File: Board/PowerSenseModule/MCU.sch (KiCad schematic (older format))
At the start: 14 parts

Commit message: Using project library
Changed library ref to project not global
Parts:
- U?: symbol MCU_Microchip_CUSTOM:dsPIC33EP32GP502_QFN -> F1_Microchip_MCUs:dsPIC33EP32GP502_QFN
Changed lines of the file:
@@
 EESchema Schematic File Version 4
+LIBS:PowerSenseModule-cache
 EELAYER 29 0
 EELAYER END
@@
 	3650 1100 3600 1100
 $Comp
-L power:GND #PWR?
+L power:GND #PWR0101
 U 1 1 5D1B4504
 P 3800 1300
-F 0 "#PWR?" H 3800 1050 50  0001 C CNN
+F 0 "#PWR0101" H 3800 1050 50  0001 C CNN
 F 1 "GND" H 3805 1127 50  0000 C CNN
 F 2 "" H 3800 1300 50  0001 C CNN
@@
 $EndComp
 $Comp
-L power:GND #PWR?
+L power:GND #PWR0102
 U 1 1 5D1BA5A8
 P 1850 2400
-F 0 "#PWR?" H 1850 2150 50  0001 C CNN
+F 0 "#PWR0102" H 1850 2150 50  0001 C CNN
 F 1 "GND" H 1855 2227 50  0000 C CNN
 F 2 "" H 1850 2400 50  0001 C CNN
@@
 Connection ~ 3600 4200
 $Comp
-L power:GND #PWR?
+L power:GND #PWR0103
 U 1 1 5D1C8BCB
 P 3600 4200
-F 0 "#PWR?" H 3600 3950 50  0001 C CNN
+F 0 "#PWR0103" H 3600 3950 50  0001 C CNN
 F 1 "GND" H 3605 4027 50  0000 C CNN
 F 2 "" H 3600 4200 50  0001 C CNN
@@
 $EndComp
 $Comp
-L power:+5V #PWR?
+L power:+5V #PWR0104
 U 1 1 5D1D3CD9
 P 7000 1000
-F 0 "#PWR?" H 7000 850 50  0001 C CNN
+F 0 "#PWR0104" H 7000 850 50  0001 C CNN
 F 1 "+5V" H 7050 1150 50  0000 C CNN
 F 2 "" H 7000 1000 50  0001 C CNN
@@
 $EndComp
 $Comp
-L power:+3.3V #PWR?
+L power:+3.3V #PWR0105
 U 1 1 5D1D4392
 P 6900 1000
-F 0 "#PWR?" H 6900 850 50  0001 C CNN
+F 0 "#PWR0105" H 6900 850 50  0001 C CNN
 F 1 "+3.3V" H 6850 1150 50  0000 C CNN
 F 2 "" H 6900 1000 50  0001 C CNN
@@
 CANL
 $Comp
-L power:GND #PWR?
+L power:GND #PWR0106
 U 1 1 5D1D8E02
 P 7000 1800
-F 0 "#PWR?" H 7000 1550 50  0001 C CNN
+F 0 "#PWR0106" H 7000 1550 50  0001 C CNN
 F 1 "GND" H 7005 1627 50  0000 C CNN
 F 2 "" H 7000 1800 50  0001 C CNN
@@
 $EndComp
 $Comp
-L power:+3.3V #PWR?
+L power:+3.3V #PWR0107
 U 1 1 5D1E7B70
 P 1850 1400
-F 0 "#PWR?" H 1850 1250 50  0001 C CNN
+F 0 "#PWR0107" H 1850 1250 50  0001 C CNN
 F 1 "+3.3V" H 1865 1573 50  0000 C CNN
 F 2 "" H 1850 1400 50  0001 C CNN
@@
 $EndComp
 $Comp
-L power:+3.3V #PWR?
+L power:+3.3V #PWR0108
 U 1 1 5D1E7EFD
 P 3300 950
-F 0 "#PWR?" H 3300 800 50  0001 C CNN
+F 0 "#PWR0108" H 3300 800 50  0001 C CNN
 F 1 "+3.3V" H 3315 1123 50  0000 C CNN
 F 2 "" H 3300 950 50  0001 C CNN
@@
 $EndComp
 $Comp
-L power:+3.3V #PWR?
+L power:+3.3V #PWR0109
 U 1 1 5D1E73B5
 P 8050 2350
-F 0 "#PWR?" H 8050 2200 50  0001 C CNN
+F 0 "#PWR0109" H 8050 2200 50  0001 C CNN
 F 1 "+3.3V" H 8065 2523 50  0000 C CNN
 F 2 "" H 8050 2350 50  0001 C CNN
@@
 Close to VDD MCU pin\n
 $Comp
-L power:GND #PWR?
+L power:GND #PWR0110
 U 1 1 5D1BE44C
 P 8050 2650
-F 0 "#PWR?" H 8050 2400 50  0001 C CNN
+F 0 "#PWR0110" H 8050 2400 50  0001 C CNN
 F 1 "GND" H 8055 2477 50  0000 C CNN
 F 2 "" H 8050 2650 50  0001 C CNN
@@
 Close to CAN transceiver
 $Comp
-L power:GND #PWR?
+L power:GND #PWR0111
 U 1 1 5D1E97C4
 P 9500 2650
-F 0 "#PWR?" H 9500 2400 50  0001 C CNN
+F 0 "#PWR0111" H 9500 2400 50  0001 C CNN
 F 1 "GND" H 9505 2477 50  0000 C CNN
 F 2 "" H 9500 2650 50  0001 C CNN
@@
 $EndComp
 $Comp
-L power:+5V #PWR?
+L power:+5V #PWR0112
 U 1 1 5D1E9E31
 P 9500 2350
-F 0 "#PWR?" H 9500 2200 50  0001 C CNN
+F 0 "#PWR0112" H 9500 2200 50  0001 C CNN
 F 1 "+5V" H 9515 2523 50  0000 C CNN
 F 2 "" H 9500 2350 50  0001 C CNN
@@
 $EndComp
 $Comp
-L power:+3.3V #PWR?
+L power:+3.3V #PWR0113
 U 1 1 5D1EE46F
 P 9100 1200
-F 0 "#PWR?" H 9100 1050 50  0001 C CNN
+F 0 "#PWR0113" H 9100 1050 50  0001 C CNN
 F 1 "+3.3V" H 9115 1373 50  0000 C CNN
 F 2 "" H 9100 1200 50  0001 C CNN
@@
 $EndComp
 $Comp
-L power:GND #PWR?
+L power:GND #PWR0114
 U 1 1 5D1EF94D
 P 9100 1450
-F 0 "#PWR?" H 9100 1200 50  0001 C CNN
+F 0 "#PWR0114" H 9100 1200 50  0001 C CNN
 F 1 "GND" H 9105 1277 50  0000 C CNN
 F 2 "" H 9100 1450 50  0001 C CNN
@@
 	9100 1400 9100 1450
 $Comp
-L power:GND #PWR?
+L power:GND #PWR0115
 U 1 1 5D1F1BB9
 P 9550 1700
-F 0 "#PWR?" H 9550 1450 50  0001 C CNN
+F 0 "#PWR0115" H 9550 1450 50  0001 C CNN
 F 1 "GND" H 9555 1527 50  0000 C CNN
 F 2 "" H 9550 1700 50  0001 C CNN
@@
 	1700 1800 1850 1800
 $Comp
-L MCU_Microchip_CUSTOM:dsPIC33EP32GP502_QFN U?
+L F1_Microchip_MCUs:dsPIC33EP32GP502_QFN U?
 U 1 1 5D1D3BA4
 P 2450 3900

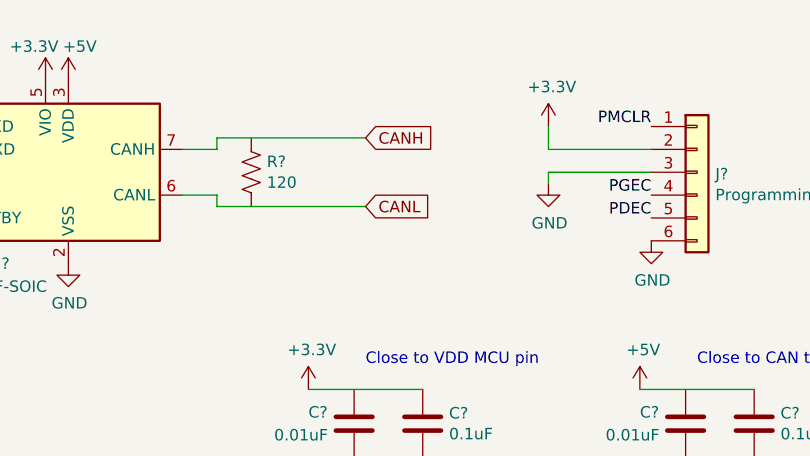
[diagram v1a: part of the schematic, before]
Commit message: Changed power connector and added CAN nets
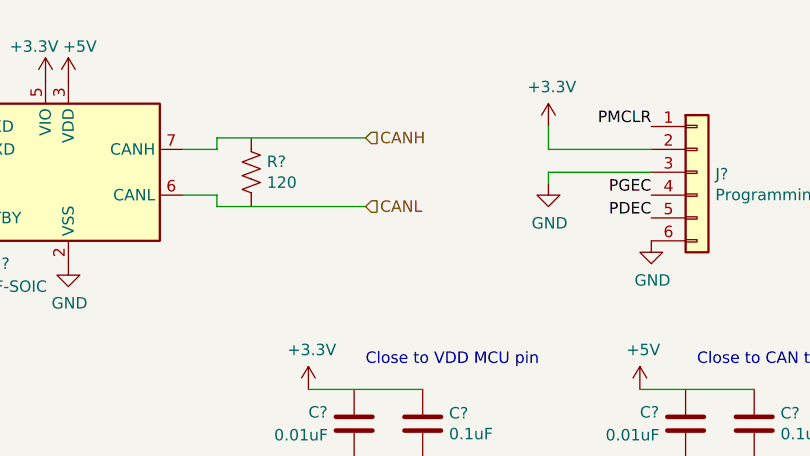
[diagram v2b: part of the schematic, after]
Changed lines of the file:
@@
 Wire Wire Line
 	7650 1500 7650 1550
-Text GLabel 8300 1250 2    50   Input ~ 0
-CANH
-Text GLabel 8300 1550 2    50   Input ~ 0
-CANL
 $Comp
 L power:GND #PWR0106
@@
 Text Label 9550 1200 2    50   ~ 0
 PMCLR
+Text HLabel 8300 1250 2    50   Input ~ 0
+CANH
+Text HLabel 8300 1550 2    50   Input ~ 0
+CANL
 $EndSCHEMATC

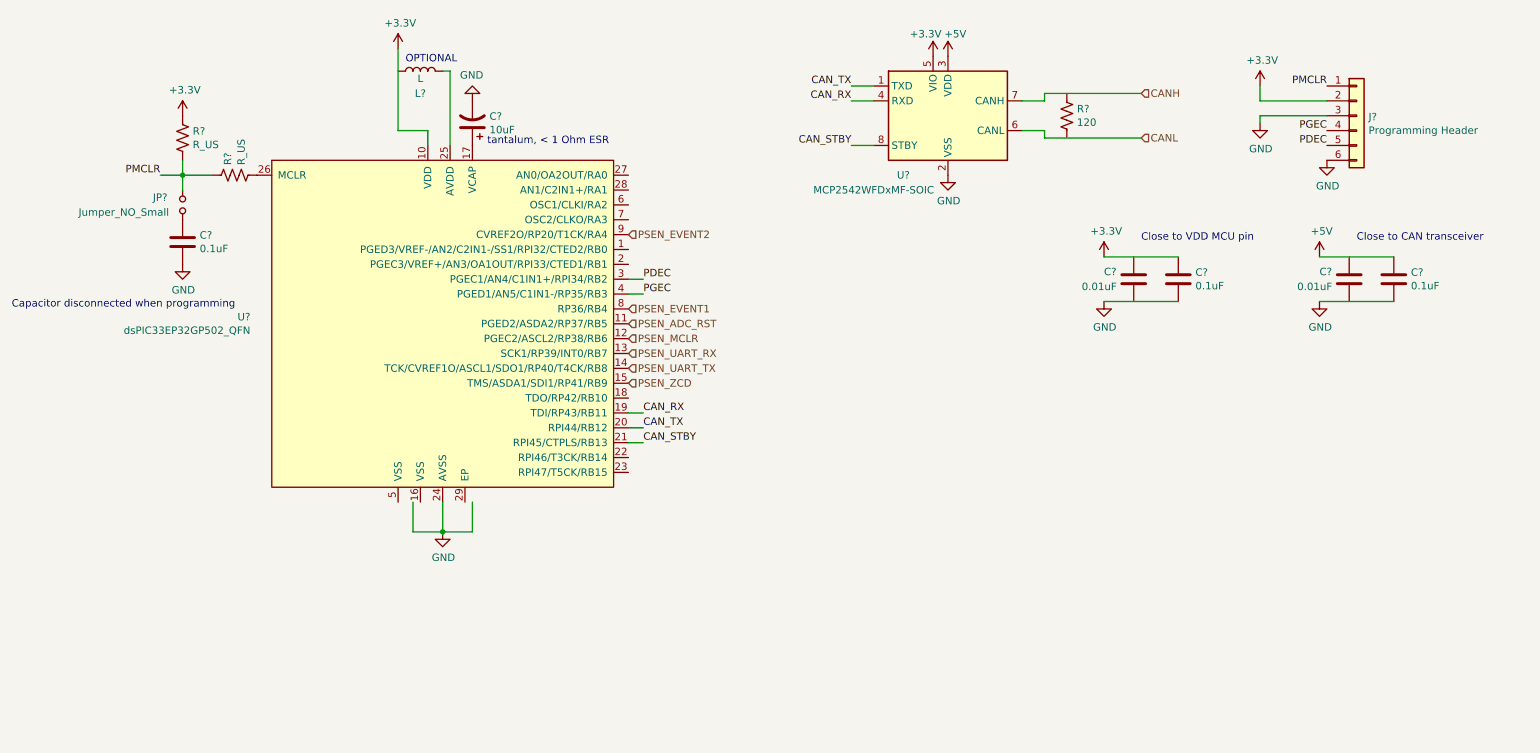
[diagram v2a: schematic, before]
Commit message: Added linear reg, cleaned up schematic
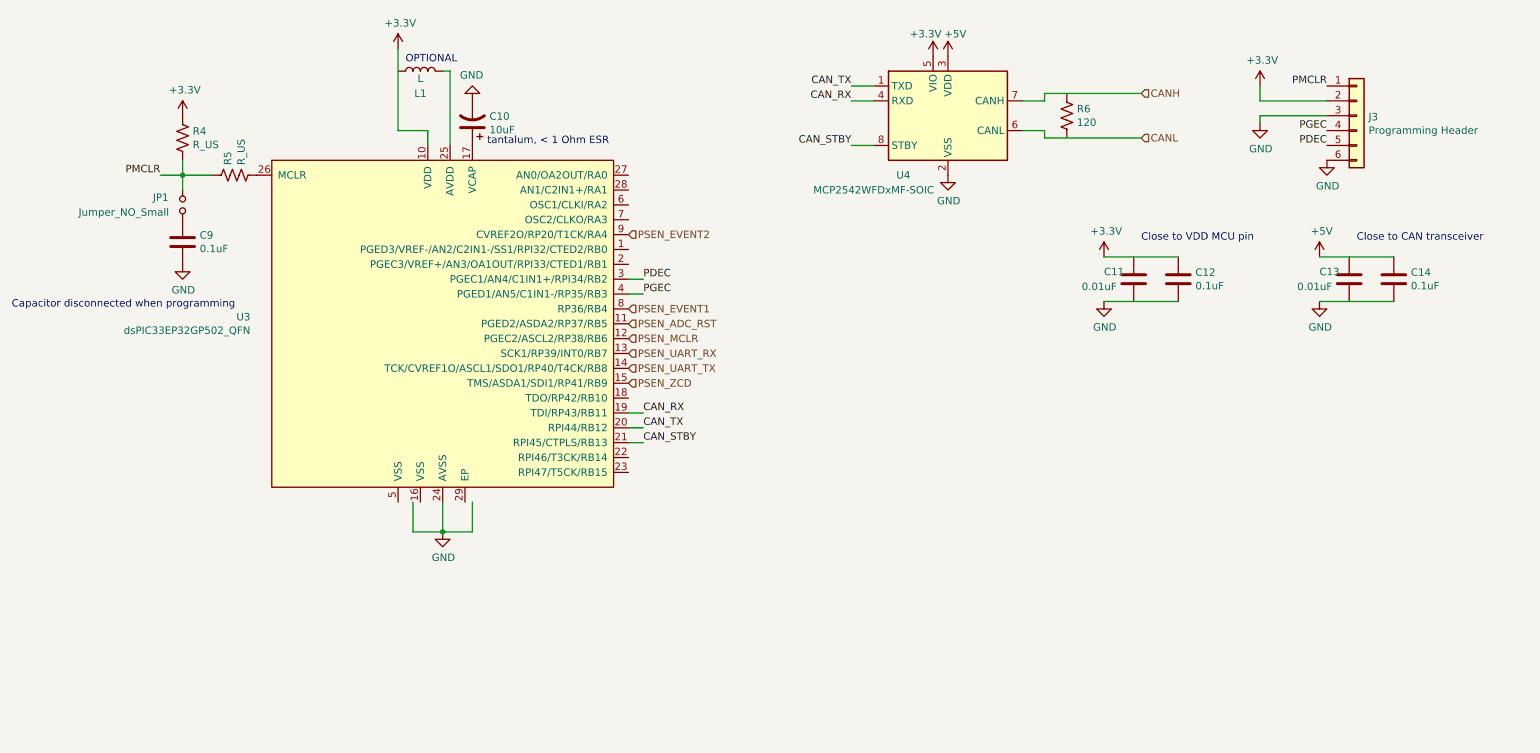
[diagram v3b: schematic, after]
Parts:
- gave numbers to parts that had none: 14
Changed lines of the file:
@@
 	3300 1500 3500 1500
 $Comp
-L Device:L L?
+L Device:L L1
 U 1 1 5D1AFDBE
 P 3450 1100
-F 0 "L?" V 3300 1100 50  0000 C CNN
+F 0 "L1" V 3300 1100 50  0000 C CNN
 F 1 "L" V 3400 1100 50  0000 C CNN
 F 2 "" H 3450 1100 50  0001 C CNN
@@
 $EndComp
 $Comp
-L Device:CP1 C?
+L Device:CP1 C10
 U 1 1 5D1B11E5
 P 3800 1450
-F 0 "C?" H 3685 1404 50  0000 R CNN
+F 0 "C10" H 3685 1404 50  0000 R CNN
 F 1 "10uF" H 3685 1495 50  0000 R CNN
 F 2 "" H 3800 1450 50  0001 C CNN
@@
 tantalum, < 1 Ohm ESR\n
 $Comp
-L Device:R_US R?
+L Device:R_US R4
 U 1 1 5D1B51D5
 P 1850 1550
-F 0 "R?" H 1918 1596 50  0000 L CNN
+F 0 "R4" H 1918 1596 50  0000 L CNN
 F 1 "R_US" H 1918 1505 50  0000 L CNN
 F 2 "" V 1890 1540 50  0001 C CNN
@@
 $EndComp
 $Comp
-L Device:R_US R?
+L Device:R_US R5
 U 1 1 5D1B85DD
 P 2200 1800
-F 0 "R?" H 2268 1846 50  0000 L CNN
+F 0 "R5" H 2268 1846 50  0000 L CNN
 F 1 "R_US" H 2268 1755 50  0000 L CNN
 F 2 "" V 2240 1790 50  0001 C CNN
@@
 	1850 1800 2050 1800
 $Comp
-L Device:Jumper_NO_Small JP?
+L Device:Jumper_NO_Small JP1
 U 1 1 5D1B8B21
 P 1850 2000
-F 0 "JP?" V 1800 1800 50  0000 L CNN
+F 0 "JP1" V 1800 1800 50  0000 L CNN
 F 1 "Jumper_NO_Small" V 1900 1300 50  0000 L CNN
 F 2 "" H 1850 2000 50  0001 C CNN
@@
 Connection ~ 1850 1800
 $Comp
-L Device:C C?
+L Device:C C9
 U 1 1 5D1BA03E
 P 1850 2250
-F 0 "C?" H 1965 2296 50  0000 L CNN
+F 0 "C9" H 1965 2296 50  0000 L CNN
 F 1 "0.1uF" H 1965 2205 50  0000 L CNN
 F 2 "" H 1888 2100 50  0001 C CNN
@@
 Capacitor disconnected when programming\n
 $Comp
-L Interface_CAN_LIN:MCP2542WFDxMF U?
+L Interface_CAN_LIN:MCP2542WFDxMF U4
 U 1 1 5D1D10B6
 P 7000 1400
-F 0 "U?" H 6700 1000 50  0000 C CNN
+F 0 "U4" H 6700 1000 50  0000 C CNN
 F 1 "MCP2542WFDxMF-SOIC" H 6500 900 50  0000 C CNN
 F 2 "Package_SO:SOIC-8_3.9x4.9mm_P1.27mm" H 7000 900 50  0001 C CIN
@@
 $EndComp
 $Comp
-L Device:R_US R?
+L Device:R_US R6
 U 1 1 5D1D5ACD
 P 7800 1400
-F 0 "R?" H 7868 1446 50  0000 L CNN
+F 0 "R6" H 7868 1446 50  0000 L CNN
 F 1 "120" H 7868 1355 50  0000 L CNN
 F 2 "" V 7840 1390 50  0001 C CNN
@@
 $EndComp
 $Comp
-L Device:C C?
+L Device:C C11
 U 1 1 5D1BE442
 P 8250 2500
-F 0 "C?" H 8050 2550 50  0000 L CNN
+F 0 "C11" H 8050 2550 50  0000 L CNN
 F 1 "0.01uF" H 7900 2450 50  0000 L CNN
 F 2 "" H 8288 2350 50  0001 C CNN
@@
 $EndComp
 $Comp
-L Device:C C?
+L Device:C C12
 U 1 1 5D1BE43C
 P 8550 2500
-F 0 "C?" H 8665 2546 50  0000 L CNN
+F 0 "C12" H 8665 2546 50  0000 L CNN
 F 1 "0.1uF" H 8665 2455 50  0000 L CNN
 F 2 "" H 8588 2350 50  0001 C CNN
@@
 $EndComp
 $Comp
-L Device:C C?
+L Device:C C13
 U 1 1 5D1E97D0
 P 9700 2500
-F 0 "C?" H 9500 2550 50  0000 L CNN
+F 0 "C13" H 9500 2550 50  0000 L CNN
 F 1 "0.01uF" H 9350 2450 50  0000 L CNN
 F 2 "" H 9738 2350 50  0001 C CNN
@@
 $EndComp
 $Comp
-L Device:C C?
+L Device:C C14
 U 1 1 5D1E97D6
 P 10000 2500
-F 0 "C?" H 10115 2546 50  0000 L CNN
+F 0 "C14" H 10115 2546 50  0000 L CNN
 F 1 "0.1uF" H 10115 2455 50  0000 L CNN
 F 2 "" H 10038 2350 50  0001 C CNN
@@
 $EndComp
 $Comp
-L Connector_Generic:Conn_01x06 J?
+L Connector_Generic:Conn_01x06 J3
 U 1 1 5D1EB185
 P 9750 1400
-F 0 "J?" H 9830 1392 50  0000 L CNN
+F 0 "J3" H 9830 1392 50  0000 L CNN
 F 1 "Programming Header" H 9830 1301 50  0000 L CNN
 F 2 "" H 9750 1400 50  0001 C CNN
@@
 	1700 1800 1850 1800
 $Comp
-L F1_Microchip_MCUs:dsPIC33EP32GP502_QFN U?
+L F1_Microchip_MCUs:dsPIC33EP32GP502_QFN U3
 U 1 1 5D1D3BA4
 P 2450 3900
-F 0 "U?" H 2306 5046 50  0000 R CNN
+F 0 "U3" H 2306 5046 50  0000 R CNN
 F 1 "dsPIC33EP32GP502_QFN" H 2306 4955 50  0000 R CNN
 F 2 "Package_DFN_QFN:QFN-28-1EP_6x6mm_P0.65mm_EP4.25x4.25mm_ThermalVias" H 2900 6550 50  0001 C CNN

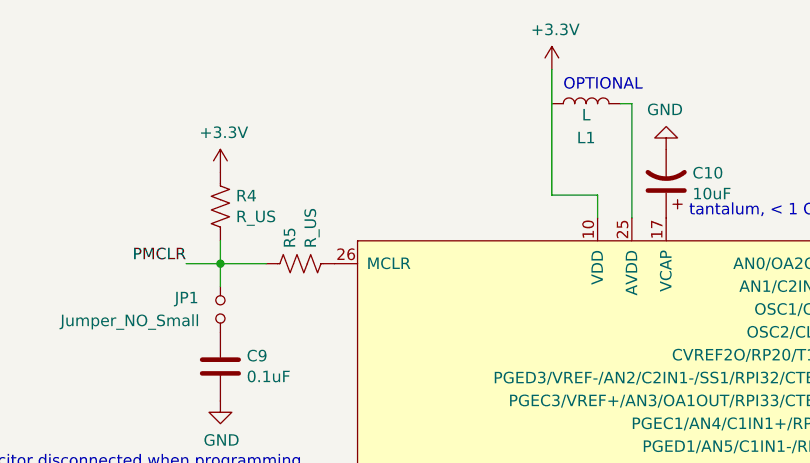
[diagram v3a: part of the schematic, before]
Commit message: Lin Reg Connected with cap, global power net, and wiring.
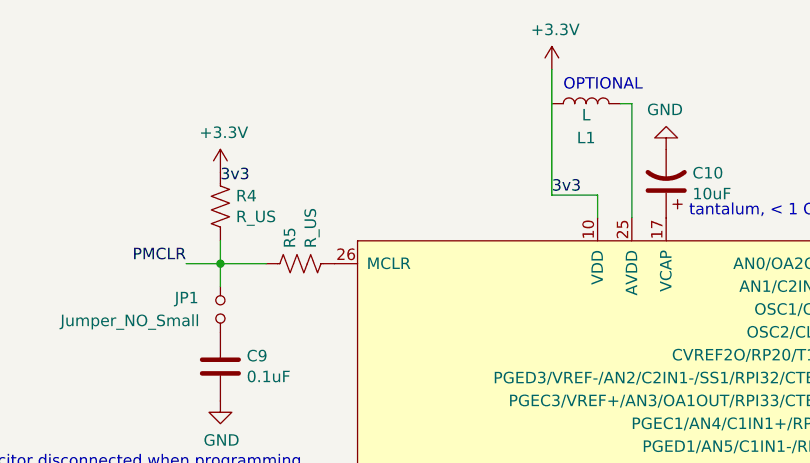
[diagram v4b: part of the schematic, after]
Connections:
- net labels added: 3v3
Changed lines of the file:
@@
 Text HLabel 8300 1550 2    50   Input ~ 0
 CANL
+Text Label 1850 1450 0    50   ~ 0
+3v3
+Text Label 3300 1500 0    50   ~ 0
+3v3
 $EndSCHEMATC

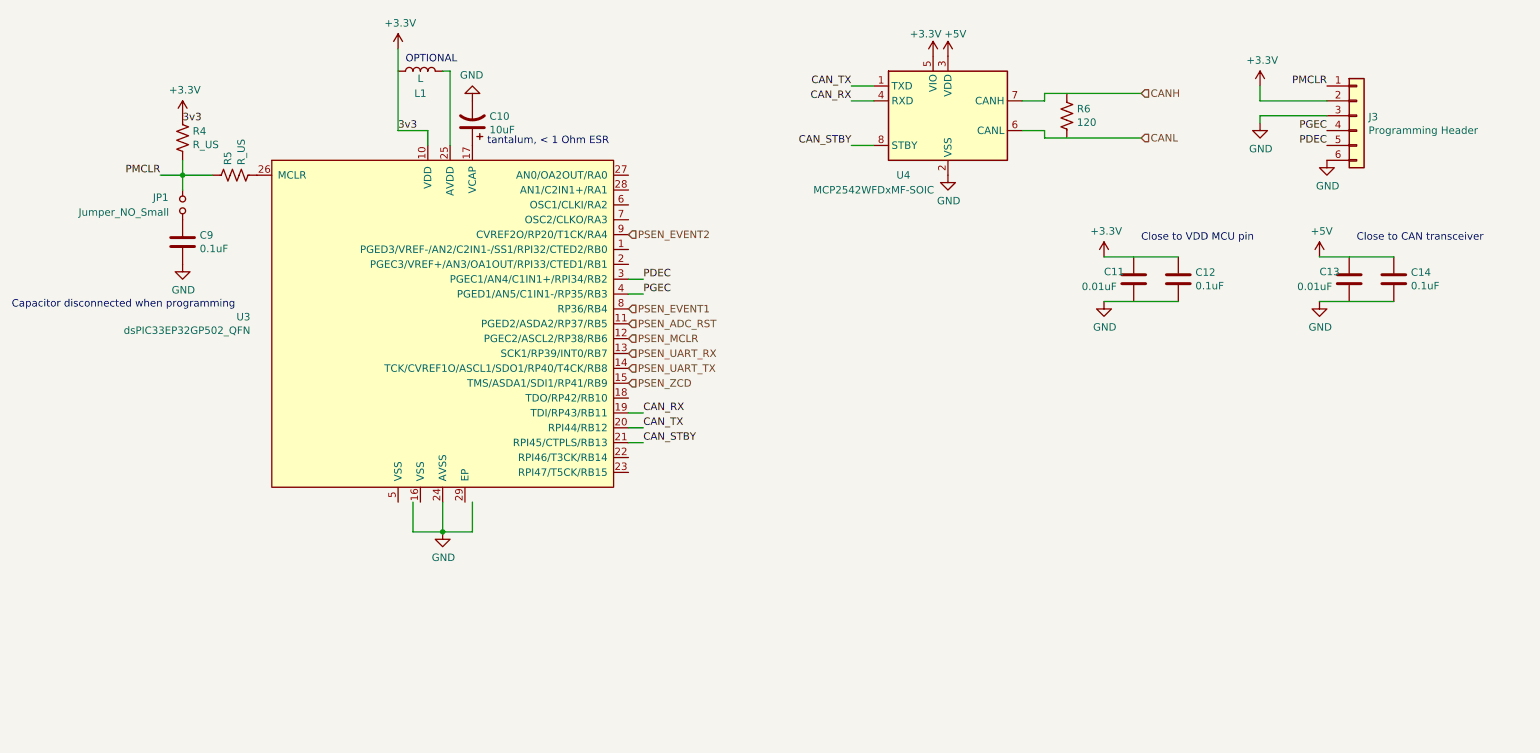
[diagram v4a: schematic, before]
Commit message: Finalizing footprints - a
Changed footprints of 4.7u, 10u, 47u ceramic caps to 0805 from 0603.

Changed output cap of linear reg to 150u electrolytic 

Added tie net for grounds

Connector footprints

Added notes

TODO:
footprints of net tie, 150u electrolytic
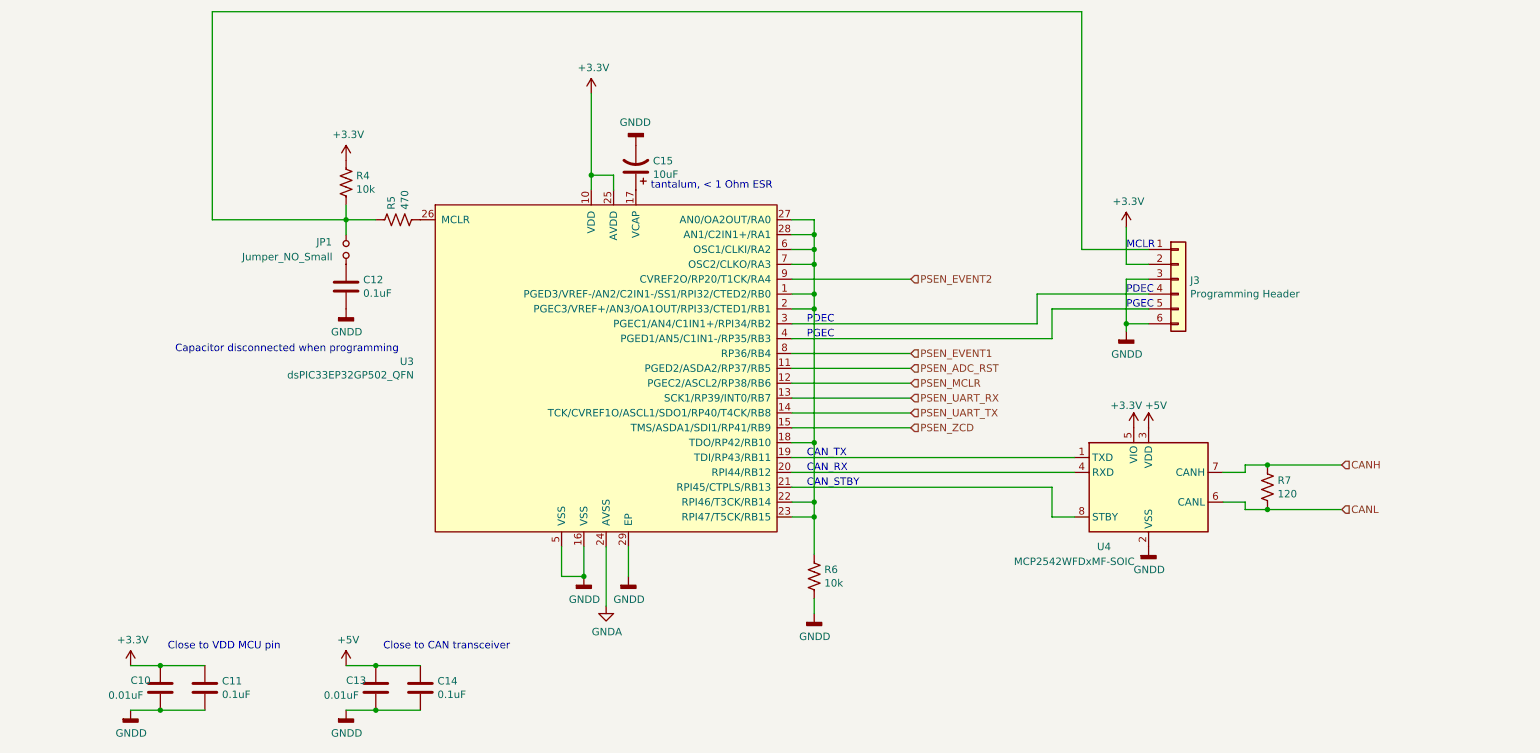
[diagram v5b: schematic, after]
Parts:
- removed L1: L, symbol Device:L
- added R6: 10k, symbol Device:R_US
- C10: renamed from C11; footprint (none) -> Capacitor_Tantalum_SMD:CP_EIA-6032-28_Kemet-C_Pad2.25x2.35mm_HandSolder
- C11: renamed from C12; footprint (none) -> Capacitor_SMD:C_0603_1608Metric_Pad1.05x0.95mm_HandSolder
- C12: renamed from C9; footprint (none) -> Capacitor_SMD:C_0603_1608Metric_Pad1.05x0.95mm_HandSolder
- C13, C14: footprint (none) -> Capacitor_SMD:C_0603_1608Metric_Pad1.05x0.95mm_HandSolder
- C15: renamed from C10; footprint (none) -> Capacitor_Tantalum_SMD:CP_EIA-6032-28_Kemet-C_Pad2.25x2.35mm_HandSolder
- J3: footprint (none) -> Connector_PinHeader_2.54mm:PinHeader_1x06_P2.54mm_Vertical
- JP1: footprint (none) -> Connector_PinHeader_2.54mm:PinHeader_1x02_P2.54mm_Vertical
- R4: value R_US -> 10k; footprint (none) -> Resistor_SMD:R_0603_1608Metric_Pad1.05x0.95mm_HandSolder
- R5: value R_US -> 470; footprint (none) -> Resistor_SMD:R_0603_1608Metric_Pad1.05x0.95mm_HandSolder
- R7: renamed from R6; footprint (none) -> Resistor_SMD:R_0603_1608Metric_Pad1.05x0.95mm_HandSolder
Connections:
- net labels added: GNDA, GNDD
- net labels removed: 3v3, CAN_RX, CAN_STBY, CAN_TX, GND, PDEC, PGEC, PMCLR
- wire segments 36 -> 76
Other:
- note added: "CAN_RX\n"
- note added: "CAN_STBY"
- note added: "CAN_TX\n"
- note added: "MCLR"
- note added: "PDEC"
- note added: "PGEC"
- note removed: "OPTIONAL\n"
- moved on the sheet: C10, C11, C12, C13, C14, C15, J3, JP1, R4, R5, R7, U3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
